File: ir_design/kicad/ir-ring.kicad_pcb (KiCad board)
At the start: 2 copper layers, 40.3 x 43.1 mm, 0 parts

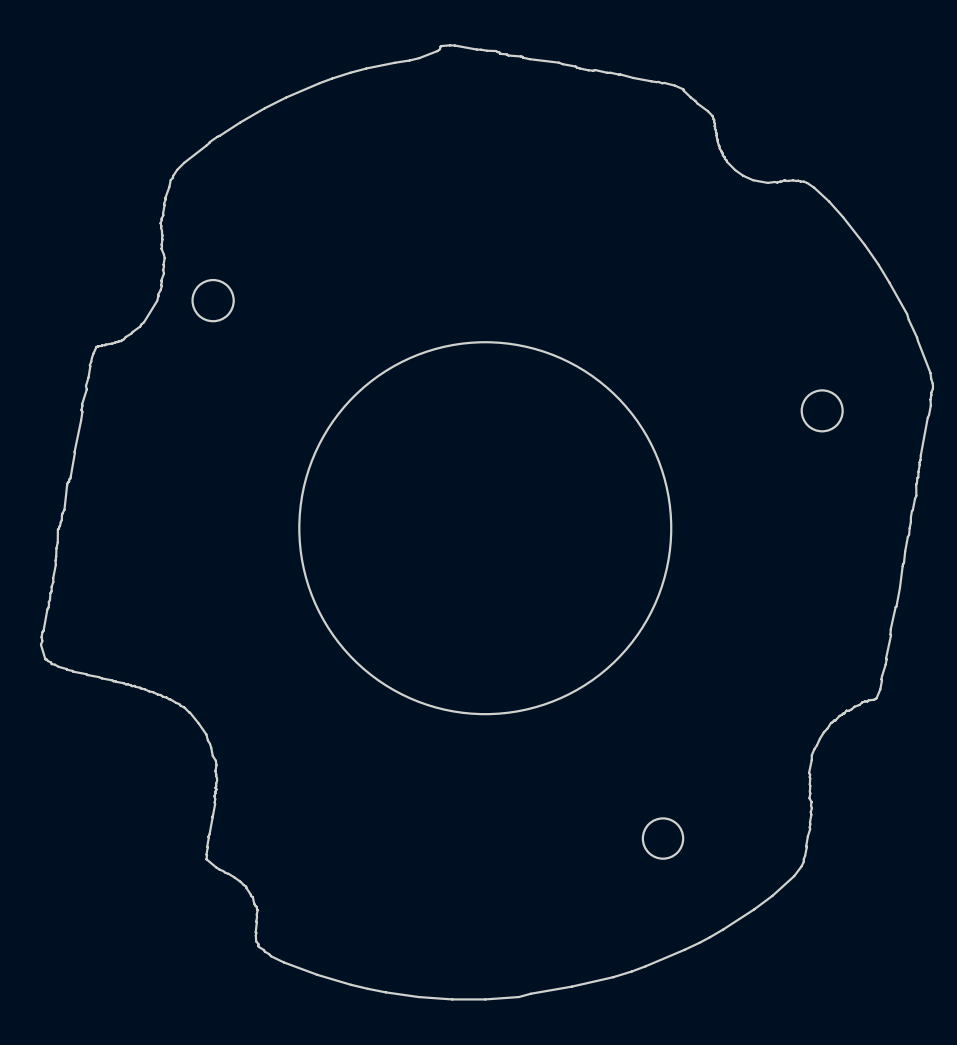
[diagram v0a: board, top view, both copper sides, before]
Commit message: feat(ir): place every footprint; J1 is 1.25 mm with a reversed pin map
09_place.py builds the whole board from scratch: outline from geometry.json,
then every footprint with its net, then assertions on the placement geometry.
pcbnew.LoadBoard() corrupts the SWIG type table in this 9.0.8 build (after
it, FootprintLoad and GetDesignSettings return bare SwigPyObjects and the
process segfaults), so the script uses CreateEmptyBoard() and never loads.

J1 correction. The earlier JST ZH 1.5 mm pick was wrong. The connector's
contacts on the back scan measure 1.246 mm pitch, and 4.98 mm between the
outer centres, so the "6 mm" was edge to edge. It is a PicoBlade-class
1.25 mm right-angle THT part with its body on the back. A footprint flipped
to the back and facing outward can only land pad 5 on the stock "+" contact,
so J1 is wired pad 5 = 5V ... pad 1 = WL_EN. The cable order is unchanged.
The script checks all five pads against the measured contacts (all within
0.03 mm) and checks that the body faces outward. Net names go on the back
silkscreen so a 1:1 overlay against the stock board confirms the mapping.

The emitters go on their measured centres, oriented so each cathode faces
the next anode. U2 goes on the stock LDR footprint at r 15.0 / 280.2 deg,
which is under the 9th dome. The converter goes on the back in the top gap:
L1 beside LX, D1 under U1, C2 on D1's cathode. The script checks SW
2.3-2.6 mm, VOUT 1.6 mm and the hot-loop return 5.1 mm. The return closes
through the F.Cu ground plane above, and an explicit check keeps the front
copper there clear; R6/R7 were moved off it to allow that.

Also: U1 moves to the standard SOT-23-6 footprint, since JLCPCB assembles
the board and hand-solder pads only cost room. Emitter thermal vias go to
0.6/0.3 mm for JLCPCB's annular-ring minimum. Schematic UUIDs are now
deterministic so footprints stay linked to their symbols across
regenerations. Reference designators move to the fab layer.

DRC: no errors. Remaining warnings a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
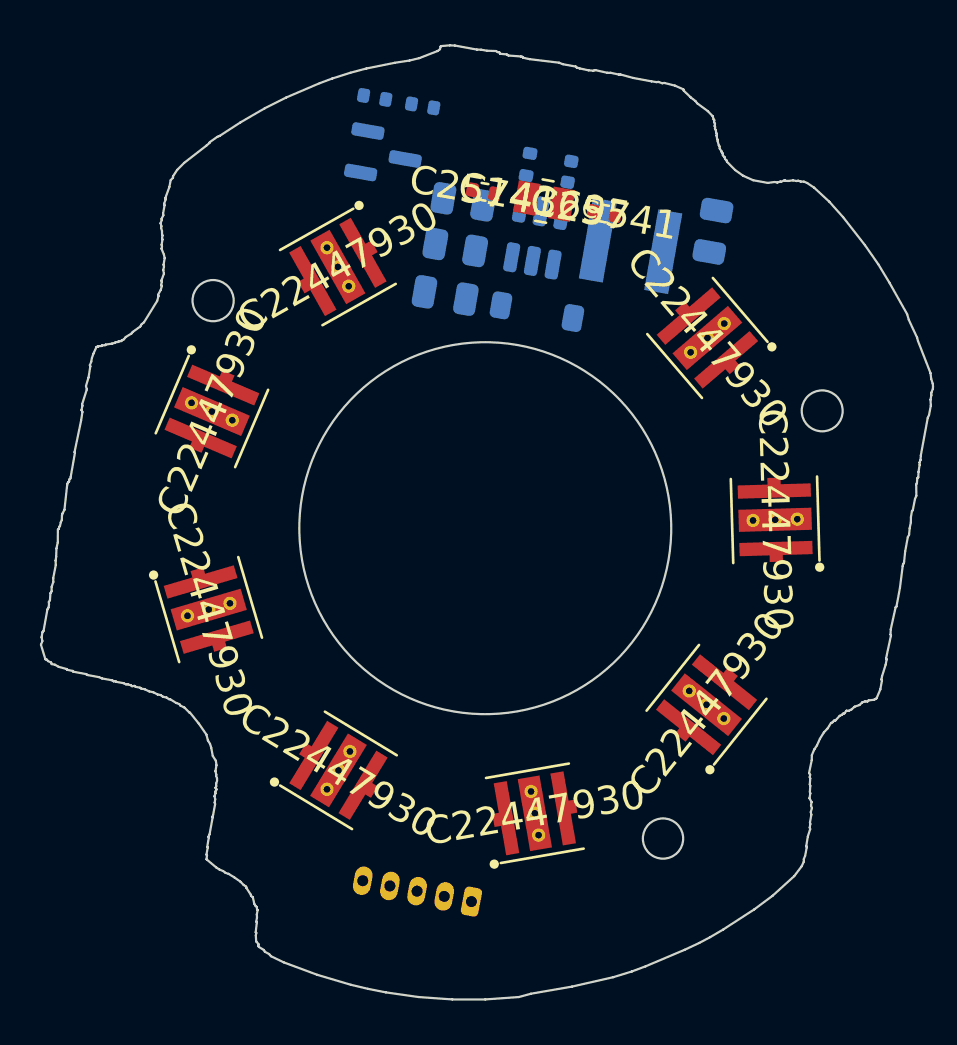
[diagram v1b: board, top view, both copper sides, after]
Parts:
- added C1: 10uF 25V, C_0805_2012Metric, B.Cu at (10.3, -13.4)
- added C2: 4.7uF 50V, C_0805_2012Metric, B.Cu at (-1.81, -10.5)
- added C3: 100nF, C_0402_1005Metric, B.Cu at (3.80, -16.1)
- added D1: >=40V 1A, D_SOD-123, B.Cu at (2.33, -9.78)
- added D2: IR 850nm 120deg, LED_3535_JNJ_EW120, F.Cu at (10.0, -8.60)
- added D3: IR 850nm 120deg, LED_3535_JNJ_EW120, F.Cu at (13.1, -0.38)
- added D4: IR 850nm 120deg, LED_3535_JNJ_EW120, F.Cu at (10.00, 7.98)
- added D5: IR 850nm 120deg, LED_3535_JNJ_EW120, F.Cu at (2.24, 12.9)
- added D6: IR 850nm 120deg, LED_3535_JNJ_EW120, F.Cu at (-6.63, 10.9)
- added D7: IR 850nm 120deg, LED_3535_JNJ_EW120, F.Cu at (-12.5, 3.68)
- added D8: IR 850nm 120deg, LED_3535_JNJ_EW120, F.Cu at (-12.4, -5.27)
- added D9: IR 850nm 120deg, LED_3535_JNJ_EW120, F.Cu at (-6.66, -11.8)
- added J1: PicoBlade/MX1.25 5p R/A THT, Molex_PicoBlade_53048-0510_1x05_P1.25mm_Horizontal, B.Cu at (-0.63, 16.9)
- added L1: 33uH SWPA4030S330MT, L_Sunlord_SWPA4030S, B.Cu at (6.56, -12.8)
- added Q1: AO3400A, SOT-23, B.Cu at (-4.54, -16.8)
- added R1a: 4.02R 1%, R_0805_2012Metric, B.Cu at (-1.36, -12.7)
- added R1b: 4.02R 1%, R_0805_2012Metric, B.Cu at (-0.99, -14.7)
- added R2: 1M, R_0402_1005Metric, B.Cu at (1.93, -16.4)
- added R3: 1k, R_0402_1005Metric, B.Cu at (-2.83, -19.1)
- added R4: 100k, R_0402_1005Metric, B.Cu at (-5.00, -19.5)
- added R6: 100k, R_0402_1005Metric, F.Cu at (-0.08, -15.2)
- added R7: 100k, R_0402_1005Metric, F.Cu at (5.37, -14.2)
- added U1: SY7200A, SOT-23-6, B.Cu at (2.33, -13.2)
- added U2: TEMT6200FX01, TEMT6200_0805, F.Cu at (2.67, -14.8)
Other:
- board text added: "5V"
- board text added: "GND"
- board text added: "IL"
- board text added: "LDR"
- board text added: "WL"

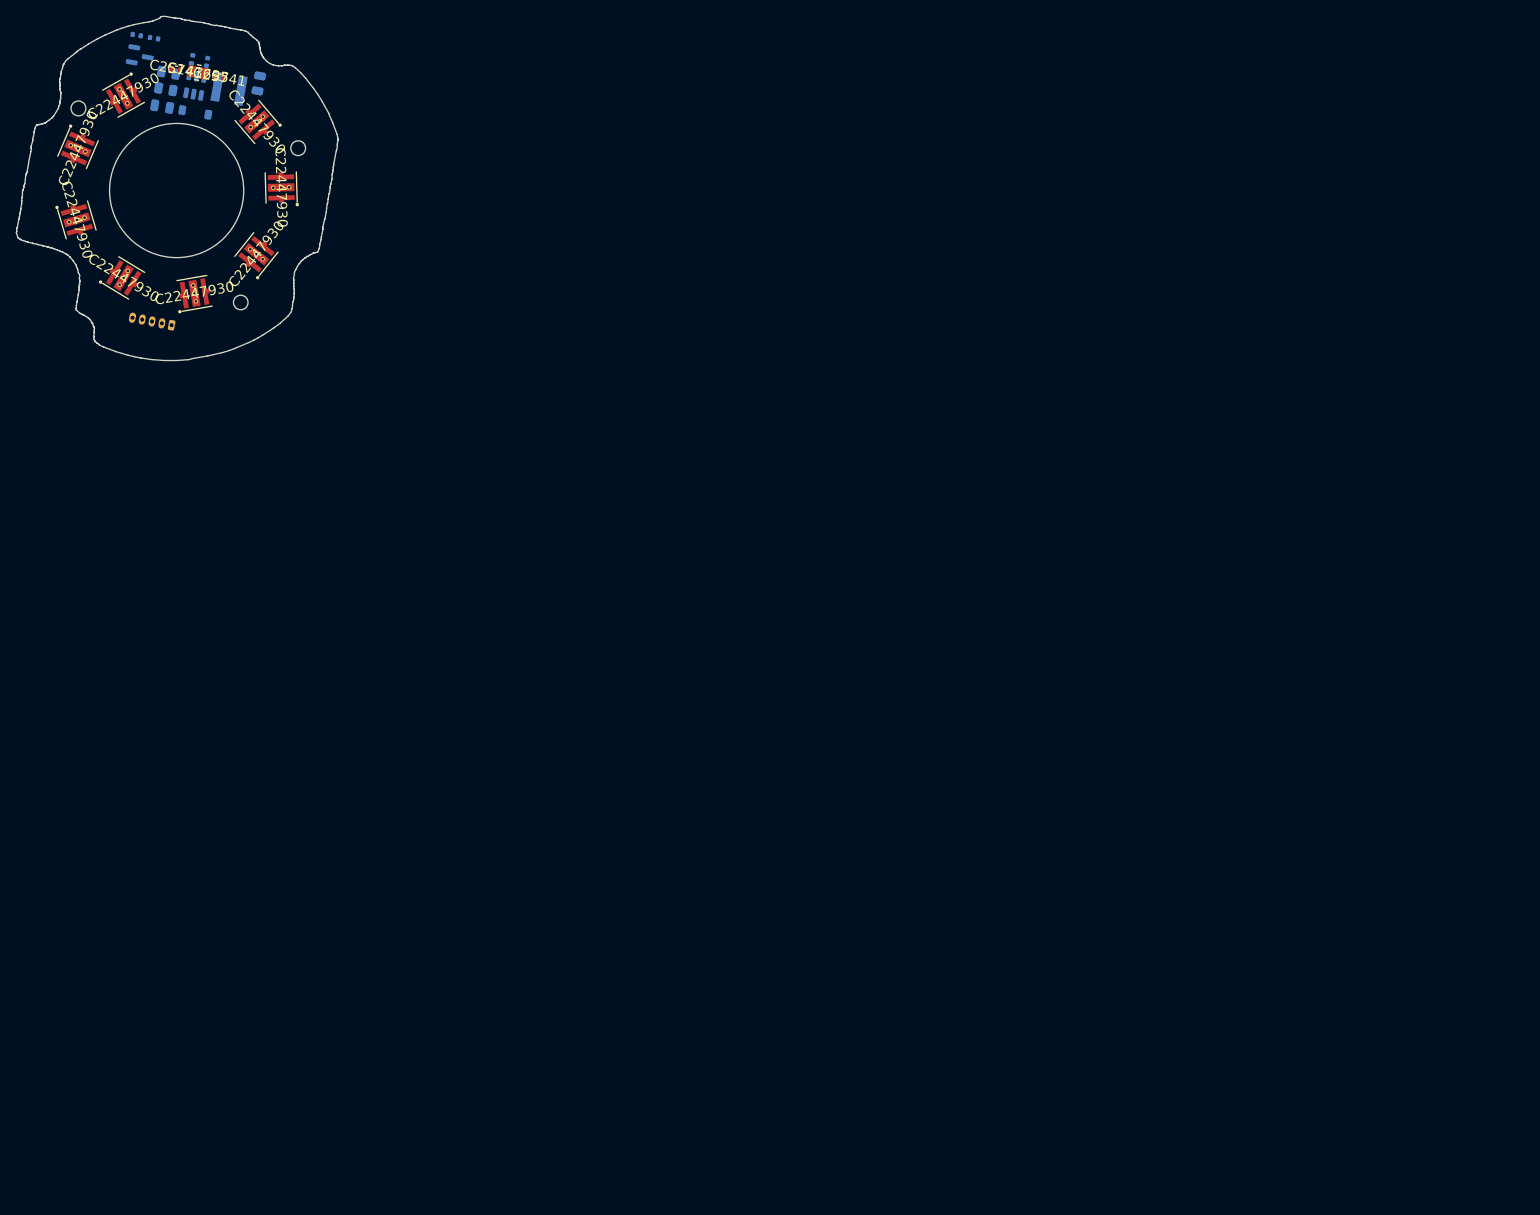
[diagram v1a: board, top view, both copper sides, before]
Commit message: feat(ir): routed board, DRC and schematic parity clean
Freerouting 2.4.1 routes the board, called directly: the MCP server wraps
the same engine and adds nothing needed. DRC with --schematic-parity exits 0
at error severity, with 0 violations, 0 unconnected pads and 0 footprint
errors, so the copper implements exactly the schematic.

Built before routing so Freerouting sees it: keepouts around the bore and the
mounting holes (3.6 mm, screw-head room); an 8-way per-emitter thermal
island on each anode net; GND pours on both layers, which Freerouting treats
as planes; and GND stitching round the outer band plus a via beside every
converter GND pad, so the hot loop returns through the plane above it. The
STR7 D8->D9 link is pre-routed along the ring, because the J1 signals cut
the D8-D9 gap and the hole keepout closes the outside. Each emitter's two
anode pads are joined on F.Cu, since they are connected only inside the
package.

Design bug caught by DRC: the thermal islands had relief spokes on the
thermal vias, which throttles the only heat path. They are now solid. J1's
GND pin goes solid too; the signals leaving beside it left room for one
spoke.

Workarounds, each documented in scripts/README.md: LoadBoard corrupts SWIG
and ZONE_FILLER crashes without it (so filling is a separate process);
DSN wiring is rewritten from route to protect; clearance gets +10 um of
margin against Freerouting's rounding; footprint LIB_IDs are set for
parity; Power clearance is 0.15 mm, which is ample at <=16 V.

Also corrects every stale JST ZH 1.5 mm J1 reference to PicoBlade 1.25 mm.

Co-Authored-By: Claude Opus 5.5 <noreply@anthropic.com>
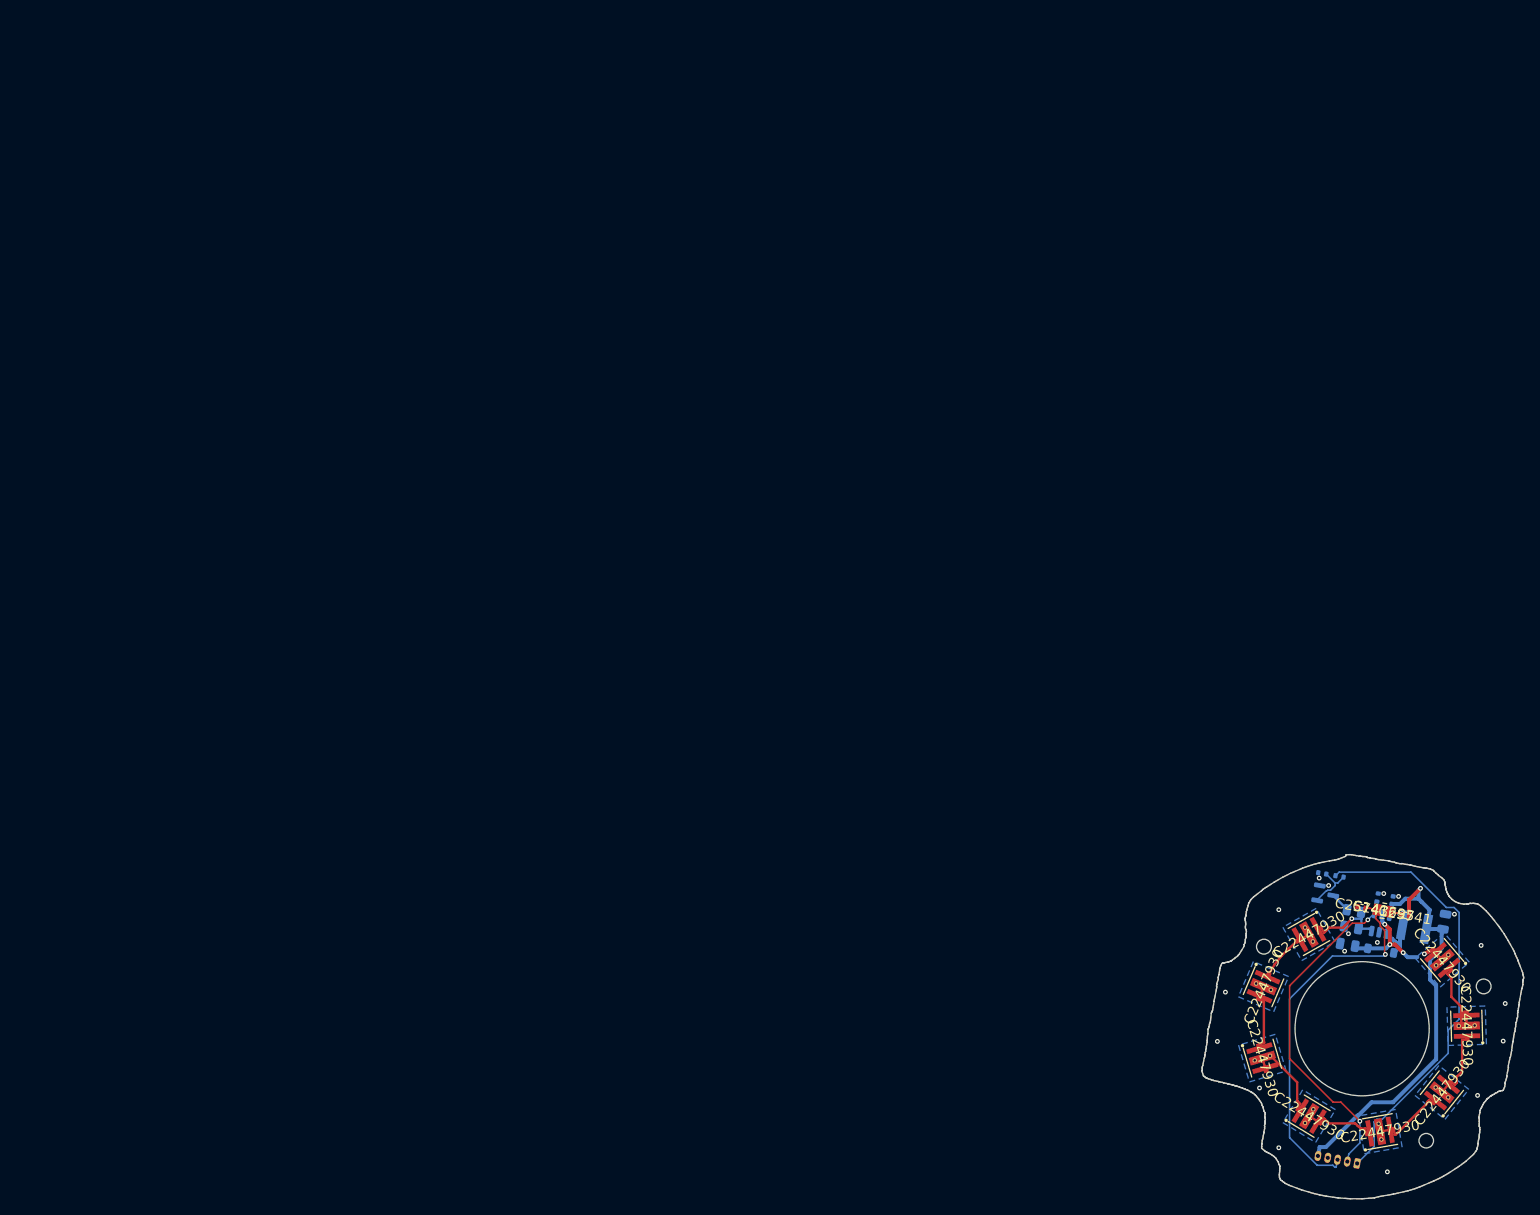
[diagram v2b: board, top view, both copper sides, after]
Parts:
- removed the R1a at (-1.36, -12.7)
- removed the R1b at (-0.99, -14.7)
- added R1a: 4.02R 1%, Resistor_SMD:R_0805_2012Metric, B.Cu at (147.1, 92.3)
- added R1b: 4.02R 1%, Resistor_SMD:R_0805_2012Metric, B.Cu at (147.5, 90.3)
- C1, C2: footprint C_0805_2012Metric -> Capacitor_SMD:C_0805_2012Metric
- C3: footprint C_0402_1005Metric -> Capacitor_SMD:C_0402_1005Metric
- D1: footprint D_SOD-123 -> Diode_SMD:D_SOD-123
- D2, D3, D4, D5, D6, D7, D8, D9: footprint LED_3535_JNJ_EW120 -> ir-ring:LED_3535_JNJ_EW120
- J1: footprint Molex_PicoBlade_53048-0510_1x05_P1.25mm_Horizontal -> Connector_Molex:Molex_PicoBlade_53048-0510_1x05_P1.25mm_Horizontal
- L1: footprint L_Sunlord_SWPA4030S -> ir-ring:L_Sunlord_SWPA4030S
- Q1: footprint SOT-23 -> Package_TO_SOT_SMD:SOT-23
- R2, R3, R4, R6, R7: footprint R_0402_1005Metric -> Resistor_SMD:R_0402_1005Metric
- U1: footprint SOT-23-6 -> Package_TO_SOT_SMD:SOT-23-6
- U2: footprint TEMT6200_0805 -> ir-ring:TEMT6200_0805
- moved C2 181.9 mm to (146.7, 94.5)
- moved U1 181.9 mm to (150.8, 91.8)
- moved R7 181.9 mm to (153.9, 90.8)
- moved R4 181.9 mm to (143.5, 85.5)
- moved Q1 181.9 mm to (144.0, 88.2)
- moved D2 181.9 mm to (158.5, 96.4)
- moved D3 181.9 mm to (161.6, 104.6)
- moved D4 181.9 mm to (158.5, 113.0)
- moved D5 181.9 mm to (150.7, 117.9)
- moved D6 181.9 mm to (141.9, 115.9)
- moved D7 181.9 mm to (136.0, 108.7)
- moved D8 181.9 mm to (136.1, 99.7)
- moved D9 181.9 mm to (141.8, 93.2)
- moved U2 181.9 mm to (151.2, 90.2)
- moved R2 181.9 mm to (150.4, 88.6)
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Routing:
- net /WL_EN: track 0.00 -> 54.9 mm
- net /+5V: track 0.00 -> 54.6 mm, vias 0 -> 1
- net /LDR: track 0.00 -> 47.6 mm, vias 0 -> 1
- net /IL_EN: track 0.00 -> 42.8 mm, vias 0 -> 2
- net /VOUT: track 0.00 -> 15.5 mm, vias 0 -> 4
- net /FB: track 0.00 -> 10.5 mm, vias 0 -> 1
- net /STR1: track 0.00 -> 10.4 mm
- net /STR5: track 0.00 -> 10.1 mm
- net /STR3: track 0.00 -> 9.79 mm
- net /STR2: track 0.00 -> 9.53 mm
- net /STR6: track 0.00 -> 9.44 mm
- net /STR4: track 0.00 -> 9.36 mm
- net /STR7: track 0.00 -> 6.68 mm
- net /SW: track 0.00 -> 6.42 mm
- net /Q1_G: track 0.00 -> 6.32 mm
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- added copper zone on B.Cu, net /GND
- added copper zone on F.Cu, net /GND
- added copper zone on B.Cu, net /STR1
- added copper zone on B.Cu, net /STR2
- added copper zone on B.Cu, net /STR3
- added copper zone on B.Cu, net /STR4
- added copper zone on B.Cu, net /STR5
- added copper zone on B.Cu, net /STR6
- added copper zone on B.Cu, net /STR7
- added copper zone on B.Cu, net /VOUT

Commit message: fix(ir): draw the schematic with wires and power symbols
The label-only sheet stacked every net name on its pin and was unreadable.
07 now lays out each block and draws real wires, junctions and +5V/GND
power symbols; 08 still diffs the result against NETS (identical), ERC clean.

Power symbols name nets globally (GND, not /GND), so 09 takes net names
from net_names.json and the committed SES/DSN are renamed to match;
DRC with --schematic-parity stays at 0 errors.

Co-Authored-By: Claude Opus 5.5 <noreply@anthropic.com>
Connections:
- net /+5V renamed +5V
- net /GND renamed GND
